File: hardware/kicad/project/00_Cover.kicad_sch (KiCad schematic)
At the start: 0 parts

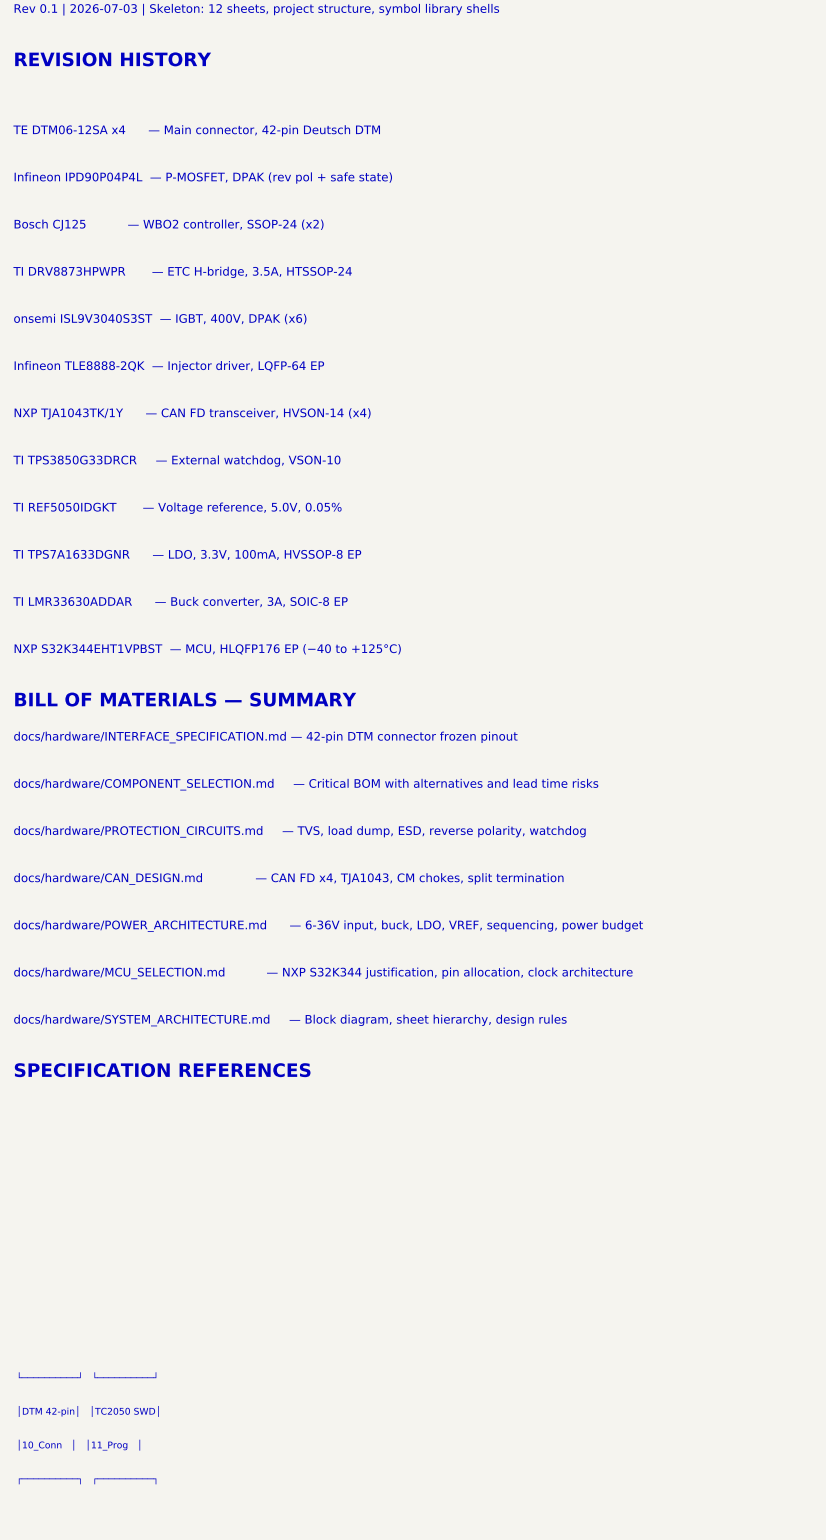
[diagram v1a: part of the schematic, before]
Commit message: fix(hardware): reconcile connector spec to 34-pin AMPSEAL, wire TP5-GND on sheet 11, add DESIGN_NOTES for known gaps
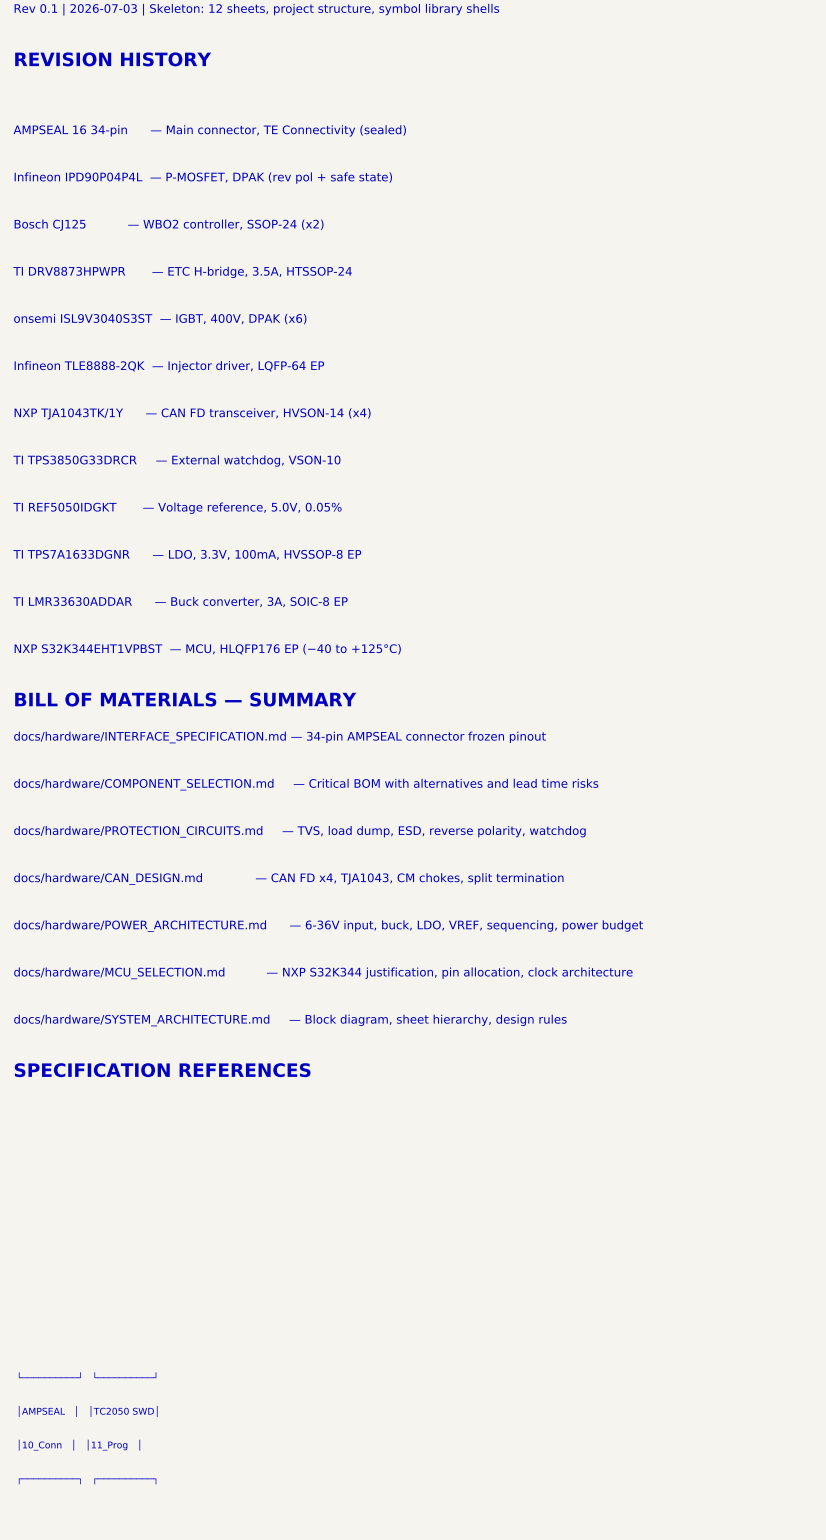
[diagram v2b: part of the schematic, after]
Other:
- note added: "AMPSEAL 16 34-pin — Main connector, TE Connectivity (sealed)"
- note added: "docs/hardware/INTERFACE_SPECIFICATION.md — 34-pin AMPSEAL connector frozen pinout"
- note added: "│AMPSEAL │ │TC2050 SWD│"
- note removed: "TE DTM06-12SA x4 — Main connector, 42-pin Deutsch DTM"
- note removed: "docs/hardware/INTERFACE_SPECIFICATION.md — 42-pin DTM connector frozen pinout"
- note removed: "│DTM 42-pin│ │TC2050 SWD│"
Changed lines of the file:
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@@
   (text " ┌──────────┐   ┌──────────┐" (at 25 130 0) (effects (font (size 1.0 1.0)) (justify left bottom)))
   (text " │10_Conn   │   │11_Prog   │" (at 25 125 0) (effects (font (size 1.0 1.0)) (justify left bottom)))
-  (text " │DTM 42-pin│   │TC2050 SWD│" (at 25 120 0) (effects (font (size 1.0 1.0)) (justify left bottom)))
+  (text " │AMPSEAL   │   │TC2050 SWD│" (at 25 120 0) (effects (font (size 1.0 1.0)) (justify left bottom)))
   (text " └──────────┘   └──────────┘" (at 25 115 0) (effects (font (size 1.0 1.0)) (justify left bottom)))
   (text "SPECIFICATION REFERENCES" (at 25 70 0) (effects (font (size 2.0 2.0) bold) (justify left bottom)))
@@
   (text "docs/hardware/PROTECTION_CIRCUITS.md     — TVS, load dump, ESD, reverse polarity, watchdog" (at 25 34 0) (effects (font (size 1.27 1.27)) (justify left bottom)))
   (text "docs/hardware/COMPONENT_SELECTION.md     — Critical BOM with alternatives and lead time risks" (at 25 27 0) (effects (font (size 1.27 1.27)) (justify left bottom)))
-  (text "docs/hardware/INTERFACE_SPECIFICATION.md — 42-pin DTM connector frozen pinout" (at 25 20 0) (effects (font (size 1.27 1.27)) (justify left bottom)))
+  (text "docs/hardware/INTERFACE_SPECIFICATION.md — 34-pin AMPSEAL connector frozen pinout" (at 25 20 0) (effects (font (size 1.27 1.27)) (justify left bottom)))
   (text "BILL OF MATERIALS — SUMMARY" (at 25 15 0) (effects (font (size 2.0 2.0) bold) (justify left bottom)))
   (text "NXP S32K344EHT1VPBST  — MCU, HLQFP176 EP (−40 to +125°C)" (at 25 7 0) (effects (font (size 1.27 1.27)) (justify left bottom)))
@@
   (text "Bosch CJ125           — WBO2 controller, SSOP-24 (x2)" (at 25 -56 0) (effects (font (size 1.27 1.27)) (justify left bottom)))
   (text "Infineon IPD90P04P4L  — P-MOSFET, DPAK (rev pol + safe state)" (at 25 -63 0) (effects (font (size 1.27 1.27)) (justify left bottom)))
-  (text "TE DTM06-12SA x4      — Main connector, 42-pin Deutsch DTM" (at 25 -70 0) (effects (font (size 1.27 1.27)) (justify left bottom)))
+  (text "AMPSEAL 16 34-pin      — Main connector, TE Connectivity (sealed)" (at 25 -70 0) (effects (font (size 1.27 1.27)) (justify left bottom)))
   (text "REVISION HISTORY" (at 25 -80 0) (effects (font (size 2.0 2.0) bold) (justify left bottom)))
   (text "Rev 0.1 | 2026-07-03 | Skeleton: 12 sheets, project structure, symbol library shells" (at 25 -88 0) (effects (font (size 1.27 1.27)) (justify left bottom)))

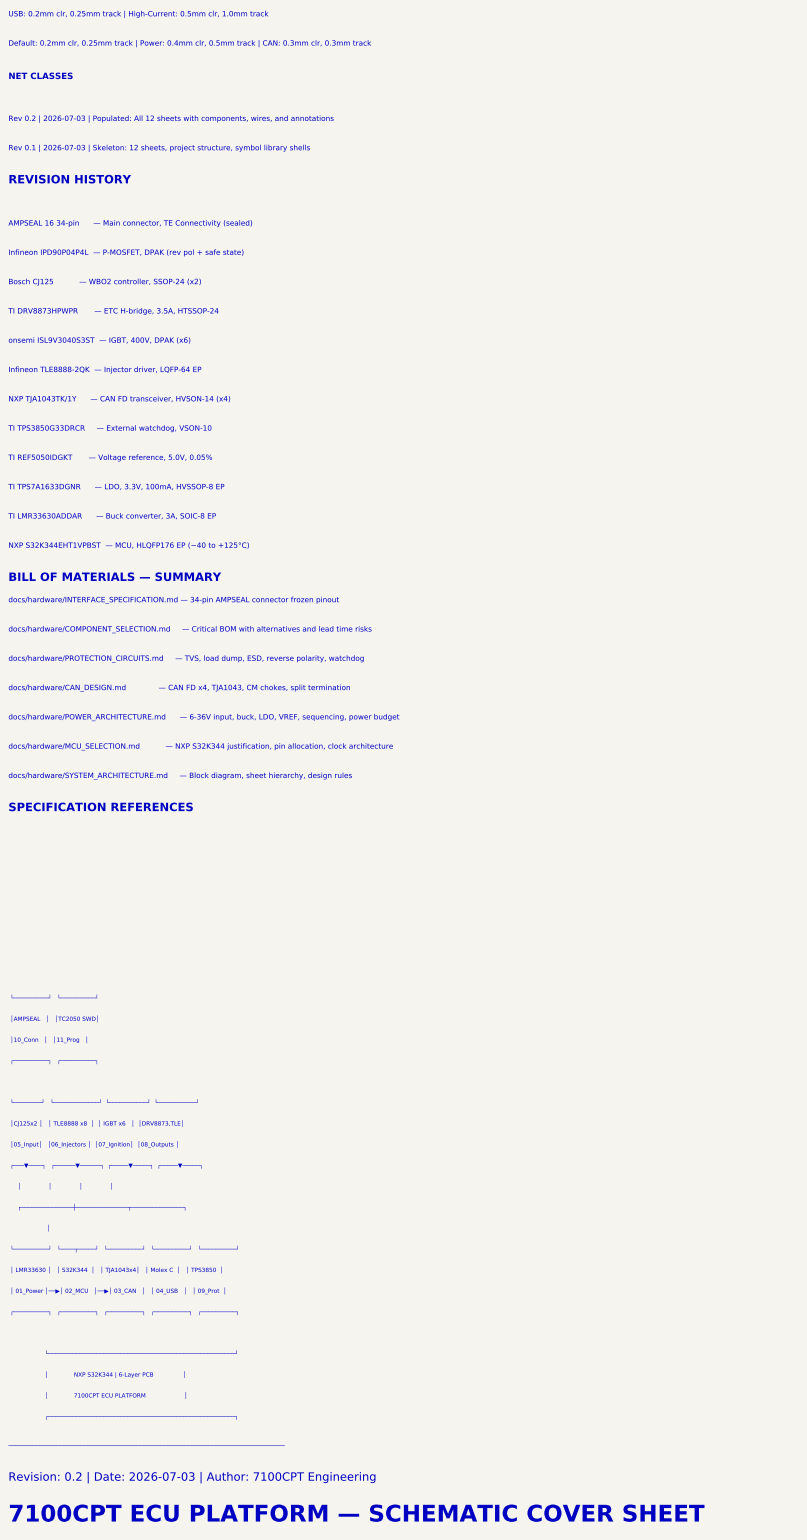
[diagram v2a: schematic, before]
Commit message: fix(hardware): ship prep — connector migration, library paths, MCU refs, Sheet 11 wiring
🔴 Connector: 42-pin Deutsch DTM → 35-pin AMPSEAL 16
  - Created AMPSEAL16_35PIN + DTM04_4PIN (WBO2) symbols in library
  - Rewrote Sheet 10 with AMPSEAL connector + WBO2 pigtail connectors
  - Updated INTERFACE_SPECIFICATION.md with full 35-pin pinout
  - Signal consolidation: dropped KNOCK2, OP, RELAY_SP; WBO2→dedicated Deutsch

🔴 Library path: sym-lib-table + fp-lib-table now point to ../ dirs
  (fixes KiCad not finding custom symbols/footprints)

🔴 MCU refs: All 11 sheets + root ECU.kicad_sch + cover ASCII art
  updated from NXP S32K344 → STM32F407VG

🟡 Sheet 11: Added global labels (+3V3, SWDIO, SWCLK, SWO, ~RESET, +5V)
  and wired TC2050 debug header through series resistors to signal nets

📄 Docs: DESIGN_PACKAGE.md, DESIGN_NOTES.md, INTERFACE_SPECIFICATION.md
  all updated to reflect current state
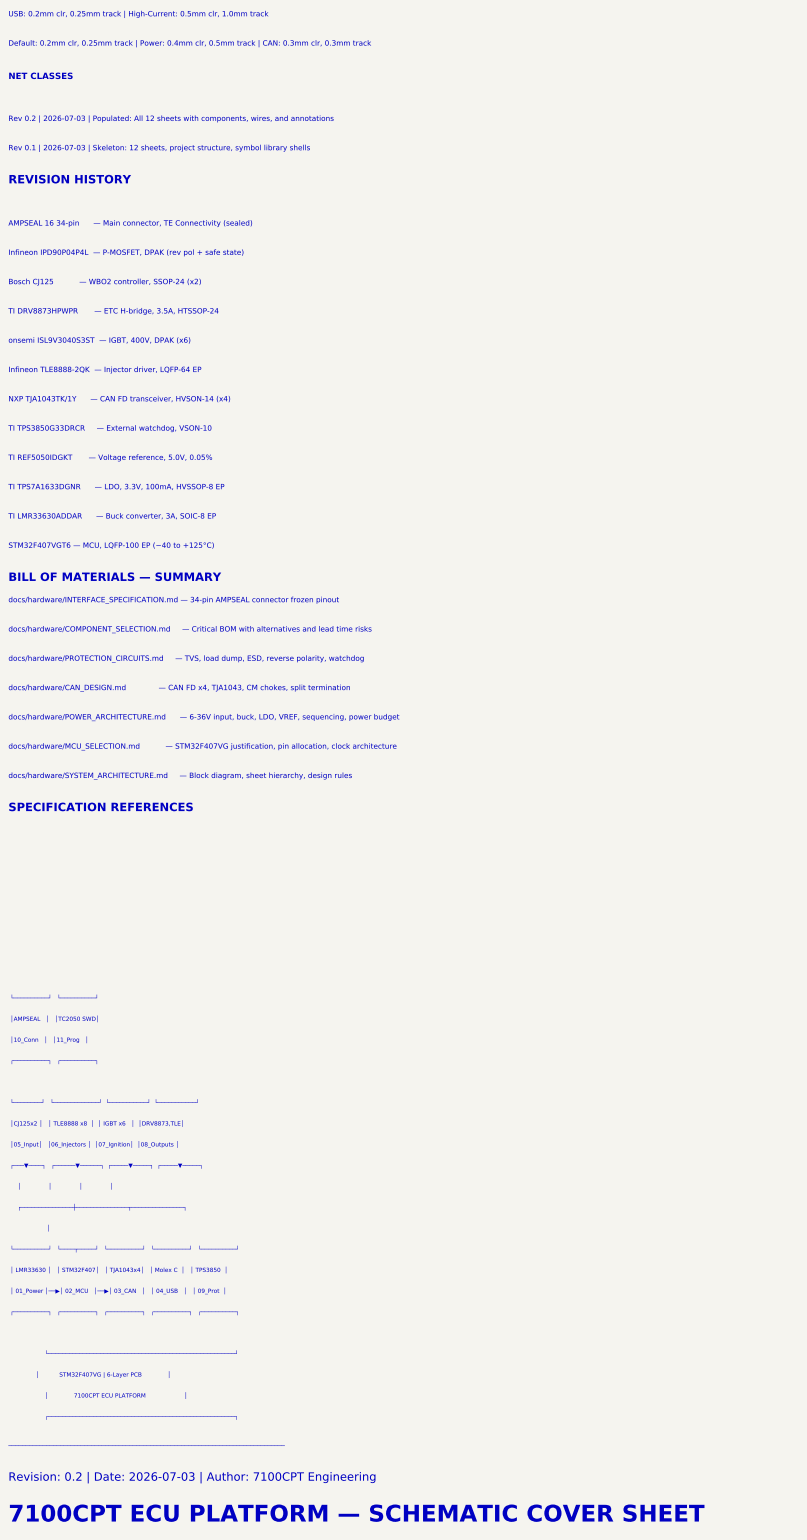
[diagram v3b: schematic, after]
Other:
- note added: "STM32F407VGT6 — MCU, LQFP-100 EP (−40 to +125°C)"
- note added: "docs/hardware/MCU_SELECTION.md — STM32F407VG justification, pin allocation, clock architecture"
- note added: "│ LMR33630 │ │ STM32F407│ │ TJA1043x4│ │ Molex C │ │ TPS3850 │"
- note added: "│ STM32F407VG | 6-Layer PCB │"
- note removed: "NXP S32K344EHT1VPBST — MCU, HLQFP176 EP (−40 to +125°C)"
- note removed: "docs/hardware/MCU_SELECTION.md — NXP S32K344 justification, pin allocation, clock architecture"
- note removed: "│ LMR33630 │ │ S32K344 │ │ TJA1043x4│ │ Molex C │ │ TPS3850 │"
- note removed: "│ NXP S32K344 | 6-Layer PCB │"
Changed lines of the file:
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@@
     (company "${COMPANY}")
     (comment 1 "Cover sheet, block diagram, BOM summary, REUSE_MATRIX reference")
-    (comment 2 "NXP S32K344 | rusEFI Firmware | IPC Class 3")
+    (comment 2 "STM32F407VG | rusEFI Firmware | IPC Class 3")
     (comment 3 "High-Tg FR-4 (TG170+) | ENIG | 1.6 mm")
     (comment 4 "Phase 0 Approved | REUSE_MATRIX gate passed")
@@
   (text "                    ┌──────────────────────────────────────────────────────┐" (at 25 215 0) (effects (font (size 1.0 1.0)) (justify left bottom)))
   (text "                    │              7100CPT ECU PLATFORM                     │" (at 25 210 0) (effects (font (size 1.0 1.0)) (justify left bottom)))
-  (text "                    │              NXP S32K344 | 6-Layer PCB                │" (at 25 205 0) (effects (font (size 1.0 1.0)) (justify left bottom)))
+  (text "               │           STM32F407VG | 6-Layer PCB              │" (at 25 205 0) (effects (font (size 1.0 1.0)) (justify left bottom)))
   (text "                    └──────────────────────────────────────────────────────┘" (at 25 200 0) (effects (font (size 1.0 1.0)) (justify left bottom)))
   (text "" (at 25 195 0) (effects (font (size 1.0 1.0)) (justify left bottom)))
   (text " ┌──────────┐   ┌──────────┐   ┌──────────┐   ┌──────────┐   ┌──────────┐" (at 25 190 0) (effects (font (size 1.0 1.0)) (justify left bottom)))
   (text " │ 01_Power │──▶│ 02_MCU   │──▶│ 03_CAN   │   │ 04_USB   │   │ 09_Prot  │" (at 25 185 0) (effects (font (size 1.0 1.0)) (justify left bottom)))
-  (text " │ LMR33630 │   │ S32K344  │   │ TJA1043x4│   │ Molex C  │   │ TPS3850  │" (at 25 180 0) (effects (font (size 1.0 1.0)) (justify left bottom)))
+  (text " │ LMR33630 │   │ STM32F407│   │ TJA1043x4│   │ Molex C  │   │ TPS3850  │" (at 25 180 0) (effects (font (size 1.0 1.0)) (justify left bottom)))
   (text " └──────────┘   └────┬─────┘   └──────────┘   └──────────┘   └──────────┘" (at 25 175 0) (effects (font (size 1.0 1.0)) (justify left bottom)))
   (text "                     │" (at 25 170 0) (effects (font (size 1.0 1.0)) (justify left bottom)))
@@
   (text "SPECIFICATION REFERENCES" (at 25 70 0) (effects (font (size 2.0 2.0) bold) (justify left bottom)))
   (text "docs/hardware/SYSTEM_ARCHITECTURE.md     — Block diagram, sheet hierarchy, design rules" (at 25 62 0) (effects (font (size 1.27 1.27)) (justify left bottom)))
-  (text "docs/hardware/MCU_SELECTION.md           — NXP S32K344 justification, pin allocation, clock architecture" (at 25 55 0) (effects (font (size 1.27 1.27)) (justify left bottom)))
+  (text "docs/hardware/MCU_SELECTION.md           — STM32F407VG justification, pin allocation, clock architecture" (at 25 55 0) (effects (font (size 1.27 1.27)) (justify left bottom)))
   (text "docs/hardware/POWER_ARCHITECTURE.md      — 6-36V input, buck, LDO, VREF, sequencing, power budget" (at 25 48 0) (effects (font (size 1.27 1.27)) (justify left bottom)))
   (text "docs/hardware/CAN_DESIGN.md              — CAN FD x4, TJA1043, CM chokes, split termination" (at 25 41 0) (effects (font (size 1.27 1.27)) (justify left bottom)))
@@
   (text "docs/hardware/INTERFACE_SPECIFICATION.md — 34-pin AMPSEAL connector frozen pinout" (at 25 20 0) (effects (font (size 1.27 1.27)) (justify left bottom)))
   (text "BILL OF MATERIALS — SUMMARY" (at 25 15 0) (effects (font (size 2.0 2.0) bold) (justify left bottom)))
-  (text "NXP S32K344EHT1VPBST  — MCU, HLQFP176 EP (−40 to +125°C)" (at 25 7 0) (effects (font (size 1.27 1.27)) (justify left bottom)))
+  (text "STM32F407VGT6 — MCU, LQFP-100 EP (−40 to +125°C)" (at 25 7 0) (effects (font (size 1.27 1.27)) (justify left bottom)))
   (text "TI LMR33630ADDAR      — Buck converter, 3A, SOIC-8 EP" (at 25 0 0) (effects (font (size 1.27 1.27)) (justify left bottom)))
   (text "TI TPS7A1633DGNR      — LDO, 3.3V, 100mA, HVSSOP-8 EP" (at 25 -7 0) (effects (font (size 1.27 1.27)) (justify left bottom)))
